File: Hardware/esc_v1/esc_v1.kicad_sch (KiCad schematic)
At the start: 19 parts, among them J1 vcc_connector, J2 SWD_tag_connect, J3 motor_connector, J4 10118193-0001LF

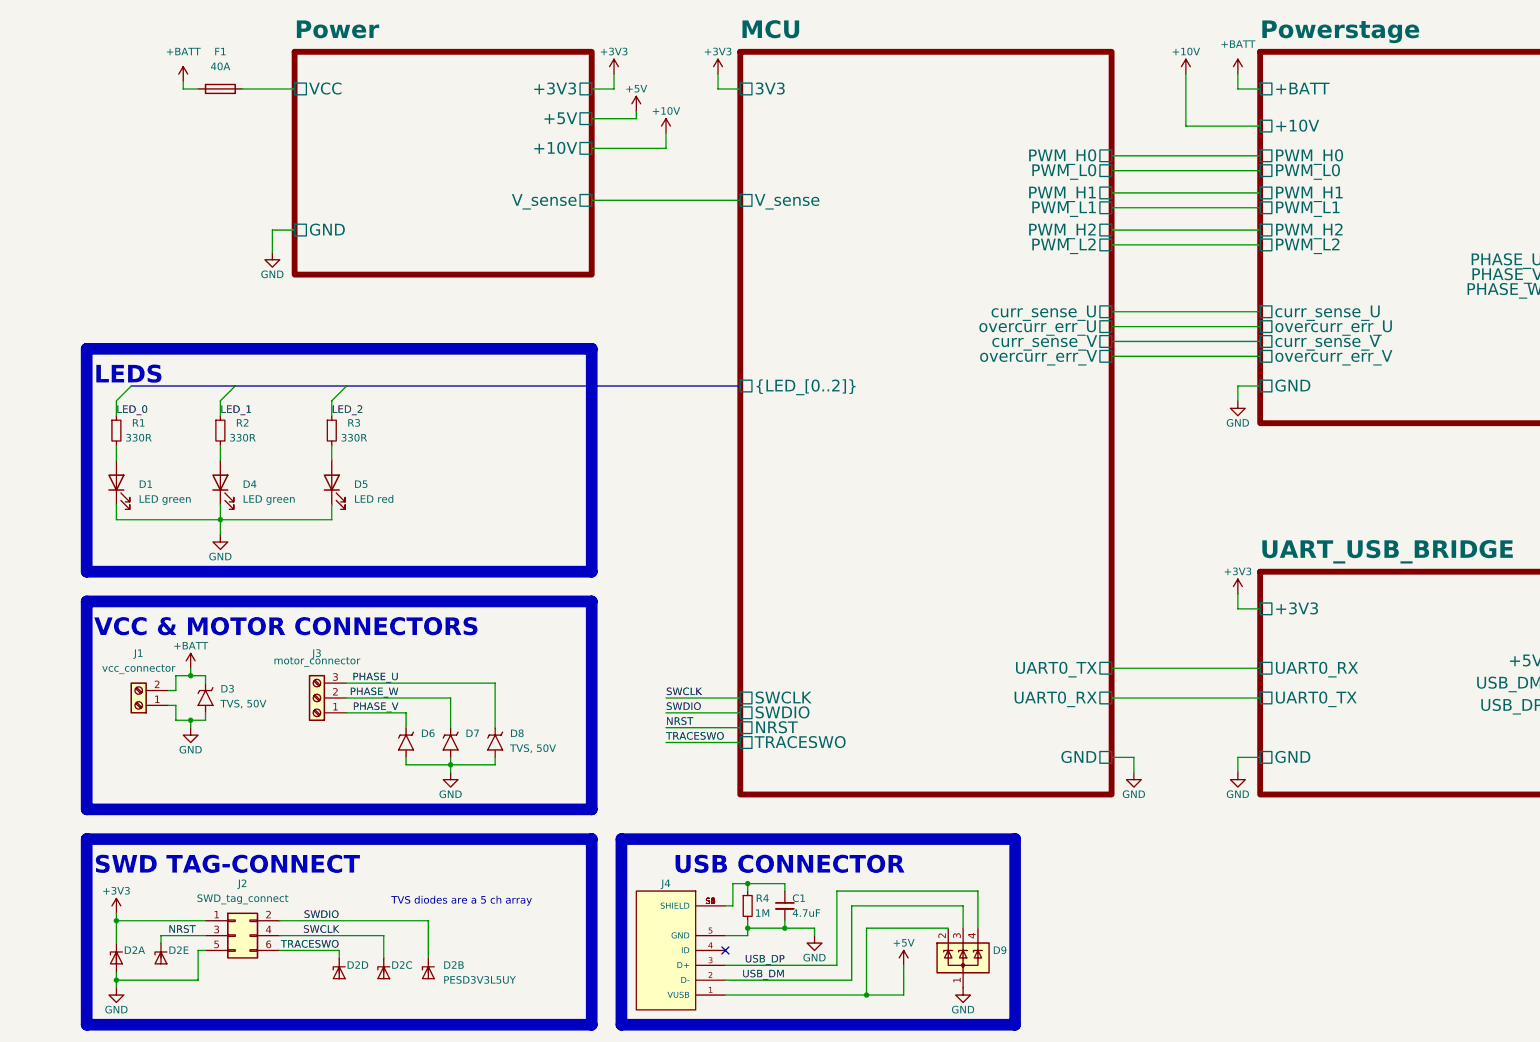
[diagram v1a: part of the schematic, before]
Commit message: changed gate driver, removed 10V buck and 5V LDO, added 5V buck. Started on Layout
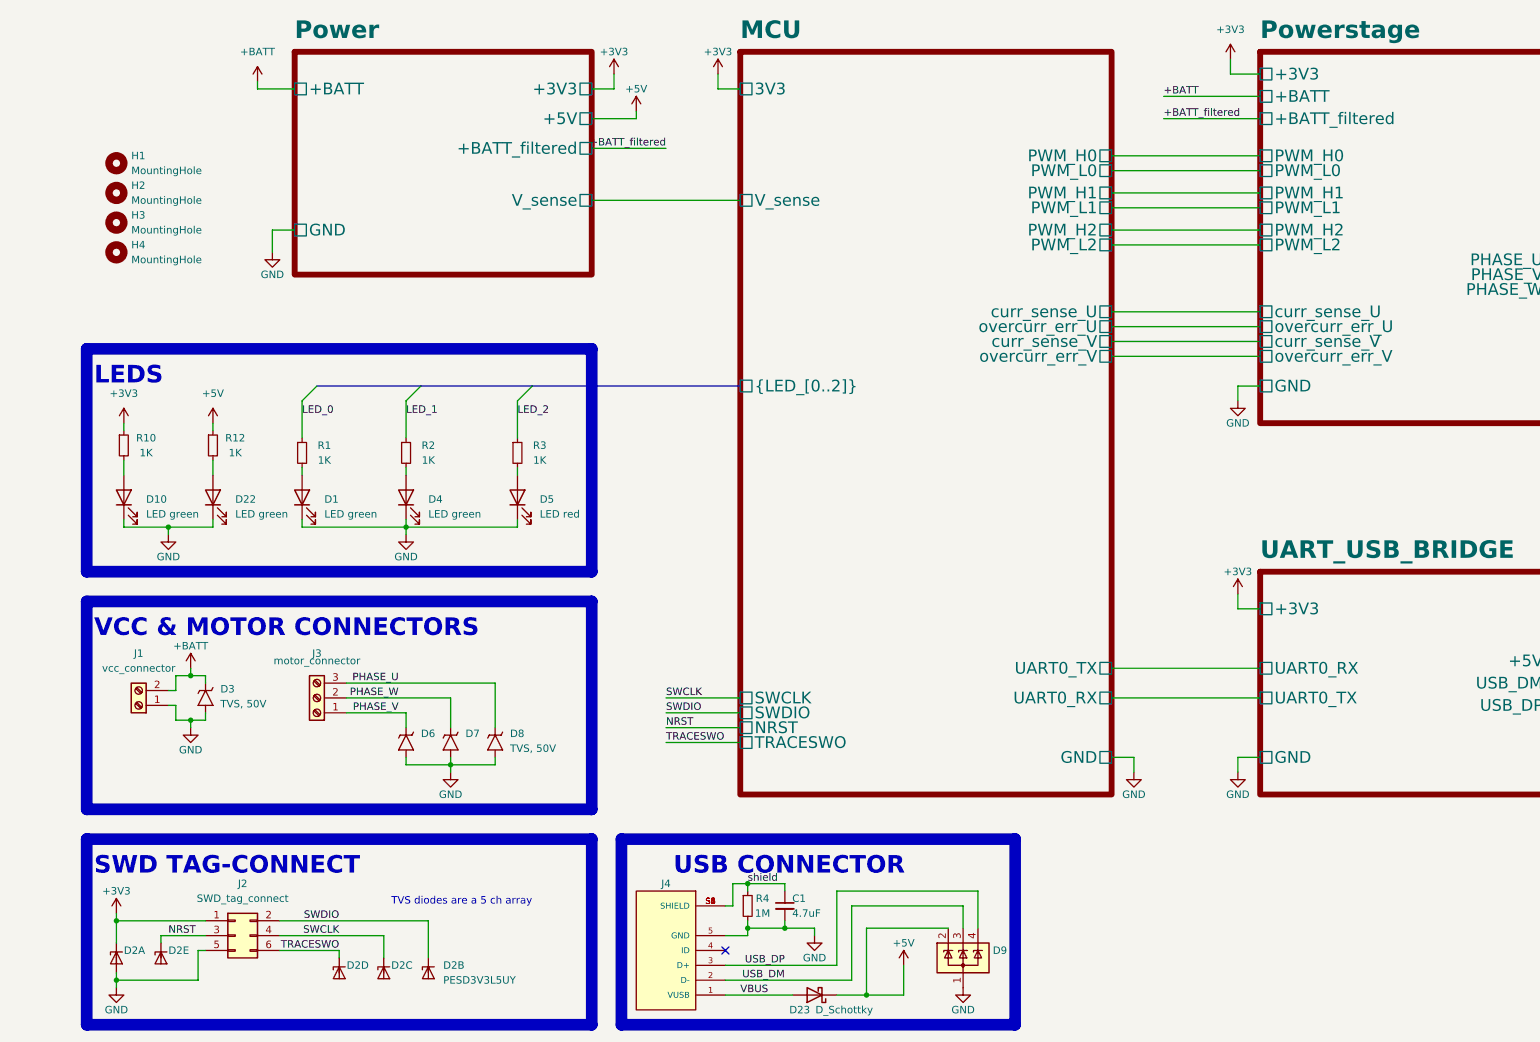
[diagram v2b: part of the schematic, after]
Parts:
- removed F1: 40A, Fuse:Fuse_1206_3216Metric, symbol Device:Fuse
- added D10, D22: LED green, LED_SMD:LED_0603_1608Metric, symbol Device:LED
- added D23: D_Schottky, Diode_SMD:D_SOD-123, symbol Device:D_Schottky
- added H1, H2, H3, H4: MountingHole, MountingHole:MountingHole_2.2mm_M2, symbol Mechanical:MountingHole
- added R10, R12: 1K, Resistor_SMD:R_0603_1608Metric, symbol Device:R_Small
- R1, R2, R3: value 330R -> 1K
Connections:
- net +3V3: now also R10.1
- net +5V: now also D23.1 (K), R12.1; no longer J4.1 (VUSB)
- net GND: now also D10.1 (K), D22.1 (K)
- net shield: now reaches C1.1, J4.S1 (SHIELD), J4.S2 (SHIELD), J4.S3 (SHIELD), J4.S4 (SHIELD), J4.S5 (SHIELD), J4.S6 (SHIELD), R4.1
- new net: D22.2 (A), R12.2
- new net: D10.2 (A), R10.2
- new net VBUS: D23.2 (A), J4.1 (VUSB)
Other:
- sheet Power ports: added +BATT, +BATT_filtered; removed +10V, VCC
- sheet Powerstage ports: added +3V3, +BATT_filtered; removed +10V
- title: ESC - Main overview -> ESC - Main sheet
- moved on the sheet: D1, D4, D5, R1, R2, R3

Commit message: Continued on layout
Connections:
- net +5V: no longer D9.2 (K)
- net VBUS: now also D9.2 (K)
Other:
- moved on the sheet: D23, D9

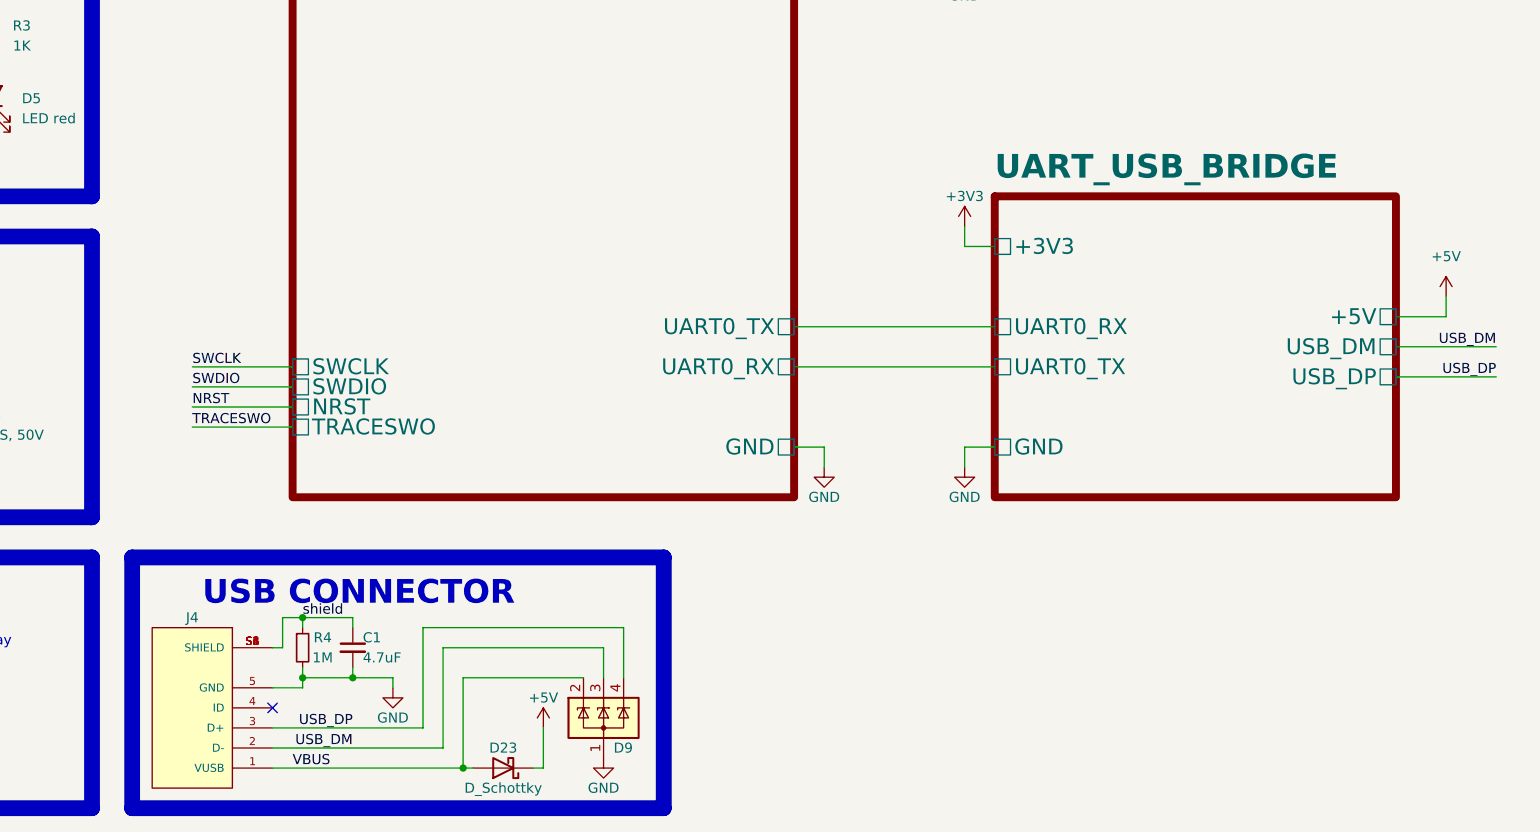
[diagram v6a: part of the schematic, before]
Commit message: Removed USB to serial chip and added serial connector. Finished layout, made production files and sent to production
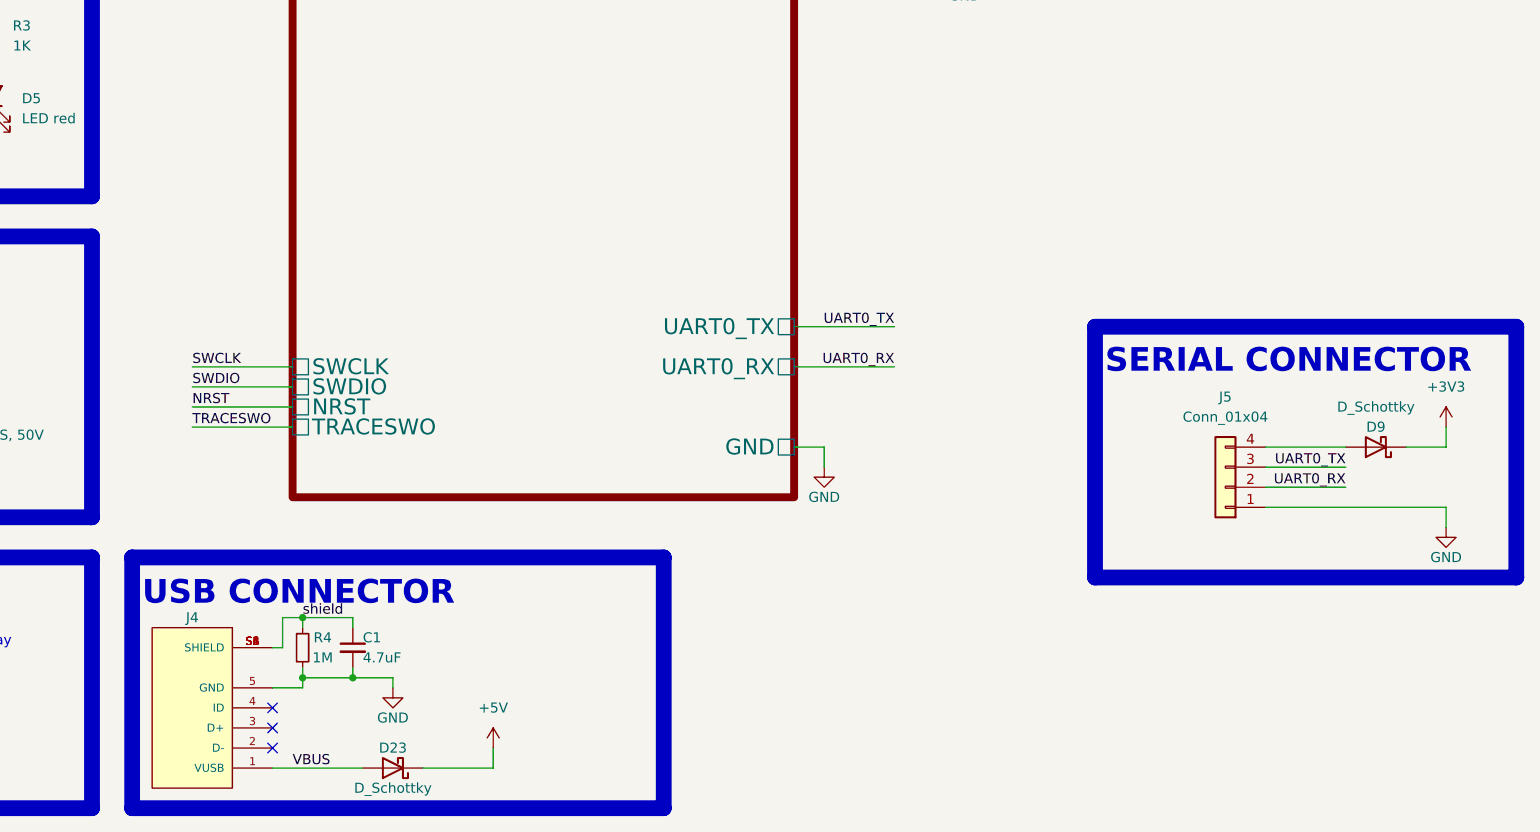
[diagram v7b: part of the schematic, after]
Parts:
- removed D9: SP0503BAHT, Package_TO_SOT_SMD:SOT-143, symbol Power_Protection:SP0503BAHT
- added D9: D_Schottky, Diode_SMD:D_SOD-123, symbol Device:D_Schottky
- added J5: Conn_01x04, Connector_PinSocket_2.54mm:PinSocket_1x04_P2.54mm_Vertical, symbol Connector_Generic:Conn_01x04
- D2: Manufcaturer_Name (none) -> Nexperia; Part no (none) -> PESD3V3L5UY
- D2: Manufcaturer_Name (none) -> Nexperia; Part no (none) -> PESD3V3L5UY; Part no.  PESD3V3L5UY,115 -> (none)
- D23: Io 1.5A -> 2A; Part no (none) -> MBR260HW; Producer (none) -> SMC Diode Solutions; Voltage rating 50V -> 60V
- D3, D6, D7, D8: Manufacturer_Name (none) -> Diodes Incorporated; Part no (none) -> SMAJ40CA-13-F
- J4: Part no (none) -> 10118193-0001LF
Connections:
- net +3V3: now also D9.1 (K)
- net GND: now also J5.1 (Pin_1)
- net USB_DM: no longer names the net of J4.2 (D-)
- net USB_DP: no longer names the net of J4.3 (D+)
- new net: D9.2 (A), J5.4 (Pin_4)
- new net UART0_RX: J5.2 (Pin_2)
- new net UART0_TX: J5.3 (Pin_3)
- no-connect marks 2 -> 4
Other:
- removed sheet UART_USB_BRIDGE
- note added: "SERIAL CONNECTOR"
- moved on the sheet: D23
